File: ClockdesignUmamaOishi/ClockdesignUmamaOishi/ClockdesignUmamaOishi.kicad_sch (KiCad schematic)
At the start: 4 parts

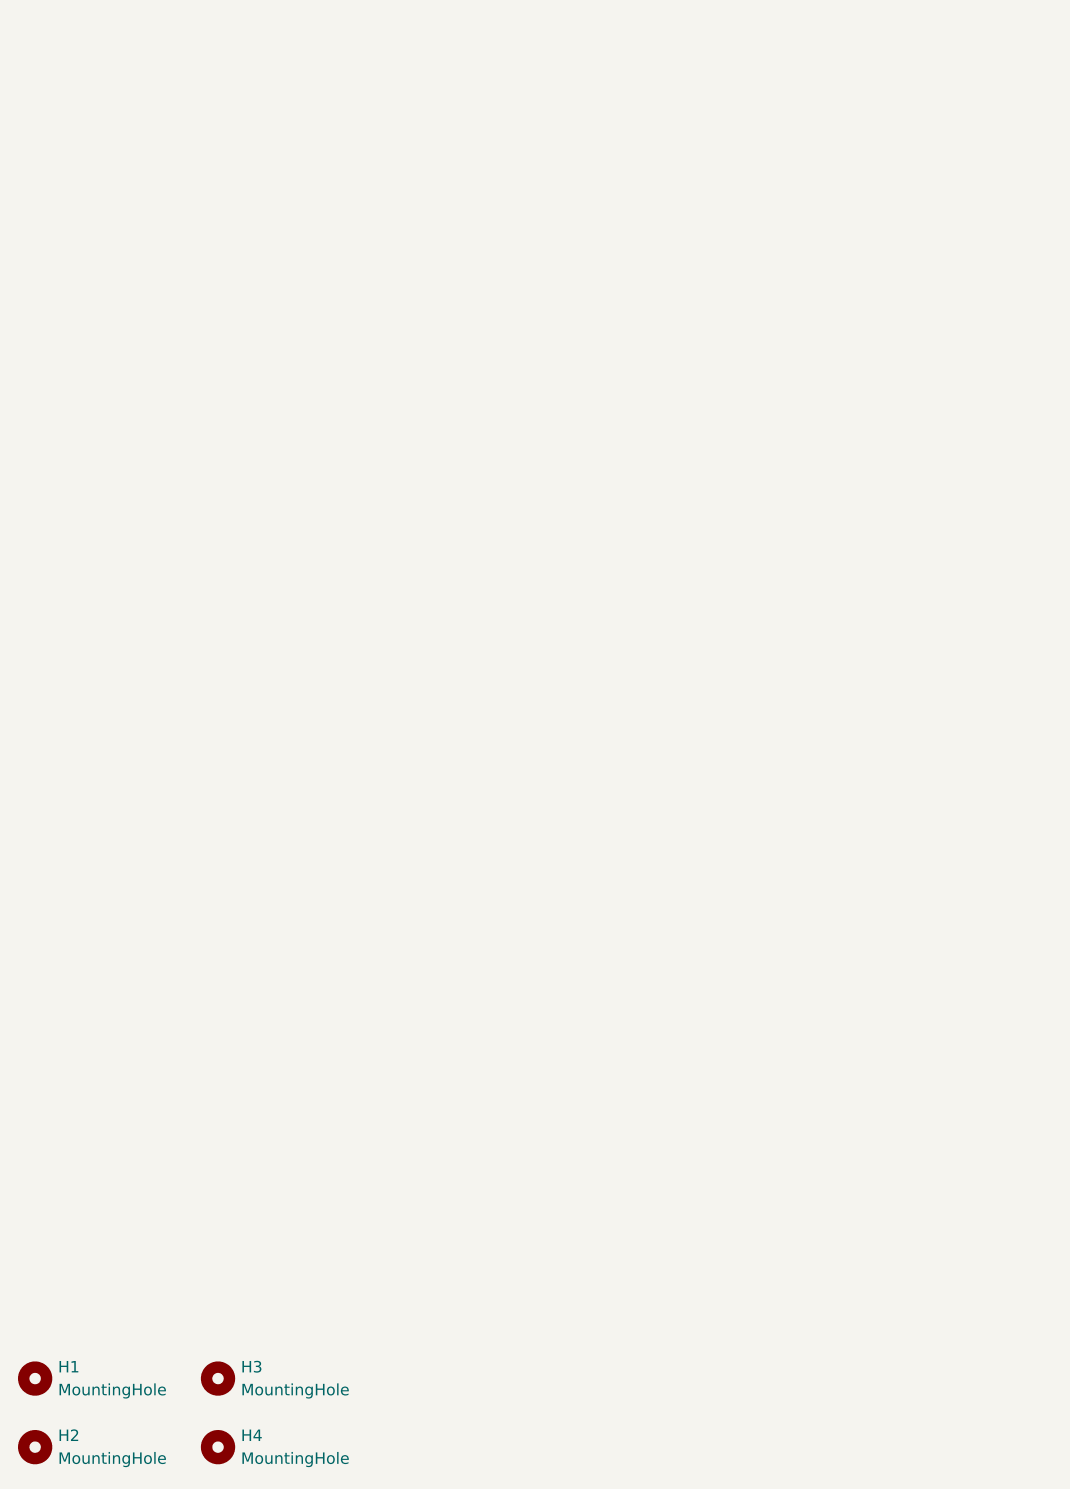
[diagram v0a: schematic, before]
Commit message: BlinkingLEDschematics
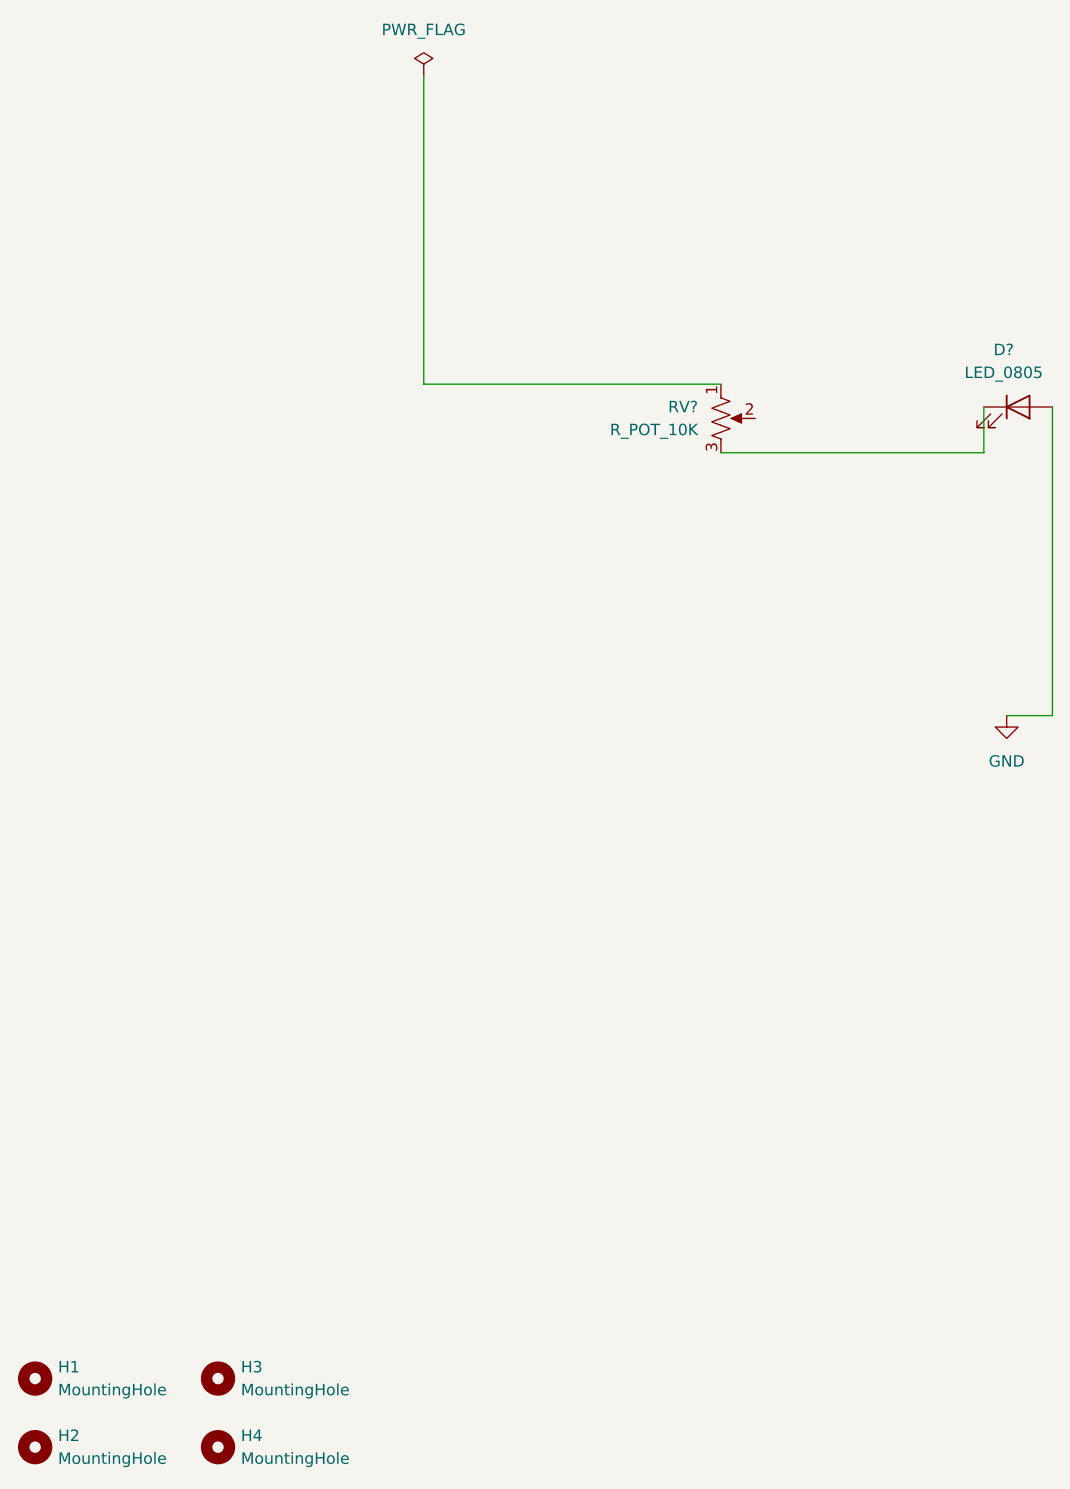
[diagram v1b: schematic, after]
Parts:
- added D?: LED_0805, footprints:LED_0805_2012Metric, symbol HPS:LED_0805
- added RV?: R_POT_10K, footprints:Potentiometer_Bourns_3386P_Vertical, symbol HPS:R_POT_10K
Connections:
- new net: D?.1 (K), RV?.3
- new net GND: D?.2 (A)
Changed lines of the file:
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@@
 (kicad_sch (version 20211123) (generator eeschema)
   (paper "A4")
+  (wire (pts (xy 68.58 34.29) (xy 68.58 68.58))
+    (stroke (width 0) (type default) (color 0 0 0 0))
+  )
+  (wire (pts (xy 68.58 68.58) (xy 101.6 68.58))
+    (stroke (width 0) (type default) (color 0 0 0 0))
+  )
+  (wire (pts (xy 138.43 105.41) (xy 133.35 105.41))
+    (stroke (width 0) (type default) (color 0 0 0 0))
+  )
+  (wire (pts (xy 101.6 76.2) (xy 130.81 76.2))
+    (stroke (width 0) (type default) (color 0 0 0 0))
+  )
+  (wire (pts (xy 138.43 71.12) (xy 138.43 105.41))
+    (stroke (width 0) (type default) (color 0 0 0 0))
+  )
+  (wire (pts (xy 130.81 76.2) (xy 130.81 71.12))
+    (stroke (width 0) (type default) (color 0 0 0 0))
+  )
   (symbol (lib_id "HPS:MountingHole") (at 45.72 179.07 0) (unit 1)
     (in_bom yes) (on_board yes) (fields_autoplaced)
@@
       (effects (font (size 1.27 1.27)) hide)
     )
+  )
+  (symbol (lib_id "HPS:R_POT_10K") (at 101.6 72.39 0) (unit 1)
+    (in_bom yes) (on_board yes) (fields_autoplaced)
+    (property "Reference" "RV?" (id 0) (at 99.06 71.1199 0)
+      (effects (font (size 1.27 1.27)) (justify right))
+    )
+    (property "Value" "R_POT_10K" (id 1) (at 99.06 73.6599 0)
+      (effects (font (size 1.27 1.27)) (justify right))
+    )
+    (property "Footprint" "footprints:Potentiometer_Bourns_3386P_Vertical" (id 2) (at 101.6 83.82 0)
+      (effects (font (size 1.27 1.27)) hide)
+    )
+    (property "Datasheet" "https://www.bourns.com/docs/Product-Datasheets/3386.pdf" (id 3) (at 101.6 72.39 0)
+      (effects (font (size 1.27 1.27)) hide)
+    )
+    (property "MFG" "Bourns Inc." (id 4) (at 101.6 78.74 0)
+      (effects (font (size 1.27 1.27)) hide)
+    )
+    (property "MPN" "3386P-1-103TLF" (id 5) (at 101.6 81.28 0)
+      (effects (font (size 1.27 1.27)) hide)
+    )
+    (property "Digikey PN" "3386P-103TLF-ND" (id 6) (at 101.6 86.36 0)
+      (effects (font (size 1.27 1.27)) hide)
+    )
+    (property "Mouser PN" "N/A" (id 7) (at 101.6 88.9 0)
+      (effects (font (size 1.27 1.27)) hide)
+    )
+    (pin "1")
+    (pin "2")
+    (pin "3")
   )
   (symbol (lib_id "HPS:MountingHole") (at 25.4 179.07 0) (unit 1)
@@
     )
   )
+  (symbol (lib_id "HPS:LED_0805") (at 134.62 71.12 0) (unit 1)
+    (in_bom yes) (on_board yes) (fields_autoplaced)
+    (property "Reference" "D?" (id 0) (at 133.0198 64.77 0))
+    (property "Value" "LED_0805" (id 1) (at 133.0198 67.31 0))
+    (property "Footprint" "footprints:LED_0805_2012Metric" (id 2) (at 135.89 82.55 0)
+      (effects (font (size 1.27 1.27)) hide)
+    )
+    (property "Datasheet" "https://www.we-online.de/katalog/datasheet/150080RS75000.pdf" (id 3) (at 134.62 71.12 0)
+      (effects (font (size 1.27 1.27)) hide)
+    )
+    (property "MFG" "Würth Elektronik" (id 4) (at 134.62 77.47 0)
+      (effects (font (size 1.27 1.27)) hide)
+    )
+    (property "MPN" "150080RS75000" (id 5) (at 134.62 80.01 0)
+      (effects (font (size 1.27 1.27)) hide)
+    )
+    (property "Digikey PN" "732-4984-1-ND" (id 6) (at 134.62 85.09 0)
+      (effects (font (size 1.27 1.27)) hide)
+    )
+    (property "Mouser PN" "N/A" (id 7) (at 134.62 87.63 0)
+      (effects (font (size 1.27 1.27)) hide)
+    )
+    (pin "1")
+    (pin "2")
+  )
+  (symbol (lib_id "HPS:PWR_FLAG") (at 68.58 34.29 0) (unit 1)
+    (in_bom yes) (on_board yes) (fields_autoplaced)
+    (property "Reference" "#FLG?" (id 0) (at 68.58 32.385 0)
+      (effects (font (size 1.27 1.27)) hide)
+    )
+    (property "Value" "PWR_FLAG" (id 1) (at 68.58 29.21 0))
+    (property "Footprint" "" (id 2) (at 68.58 34.29 0)
+      (effects (font (size 1.27 1.27)) hide)
+    )
+    (property "Datasheet" "~" (id 3) (at 68.58 34.29 0)
+      (effects (font (size 1.27 1.27)) hide)
+    )
+    (pin "1")
+  )
   (symbol (lib_id "HPS:MountingHole") (at 25.4 186.69 0) (unit 1)
     (in_bom yes) (on_board yes) (fields_autoplaced)
@@
       (effects (font (size 1.27 1.27)) hide)
     )
+  )
+  (symbol (lib_id "HPS:GND") (at 133.35 105.41 0) (unit 1)
+    (in_bom yes) (on_board yes) (fields_autoplaced)
+    (property "Reference" "#PWR?" (id 0) (at 133.35 111.76 0)
+      (effects (font (size 1.27 1.27)) hide)
+    )
+    (property "Value" "GND" (id 1) (at 133.35 110.49 0))
+    (property "Footprint" "" (id 2) (at 133.35 105.41 0)
+      (effects (font (size 1.27 1.27)) hide)
+    )
+    (property "Datasheet" "" (id 3) (at 133.35 105.41 0)
+      (effects (font (size 1.27 1.27)) hide)
+    )
+    (pin "1")
   )
   (symbol (lib_id "HPS:MountingHole") (at 45.72 186.69 0) (unit 1)
@@
   )
   (symbol_instances
+    (path "/ab28e42a-6d5c-4889-9736-6f98cf67a0fd"
+      (reference "#FLG?") (unit 1) (value "PWR_FLAG") (footprint "")
+    )
+    (path "/f43db61d-8306-430e-a747-ff62125583dd"
+      (reference "#PWR?") (unit 1) (value "GND") (footprint "")
+    )
+    (path "/79eb430e-278e-4e5c-8c2e-84230a7368b5"
+      (reference "D?") (unit 1) (value "LED_0805") (footprint "footprints:LED_0805_2012Metric")
+    )
     (path "/3078fc62-fc65-44c3-8730-e98e32046f59"
       (reference "H1") (unit 1) (value "MountingHole") (footprint "footprints:MountingHole_3.2mm_M3")
@@
       (reference "H4") (unit 1) (value "MountingHole") (footprint "footprints:MountingHole_3.2mm_M3")
     )
+    (path "/2a2c4afe-073d-4e99-ab1b-eec305d09914"
+      (reference "RV?") (unit 1) (value "R_POT_10K") (footprint "footprints:Potentiometer_Bourns_3386P_Vertical")
+    )
   )
